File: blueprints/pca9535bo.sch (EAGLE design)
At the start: 8 parts, among them IC1 PCA9535D, J1 0R, J2 0R, J3 0R

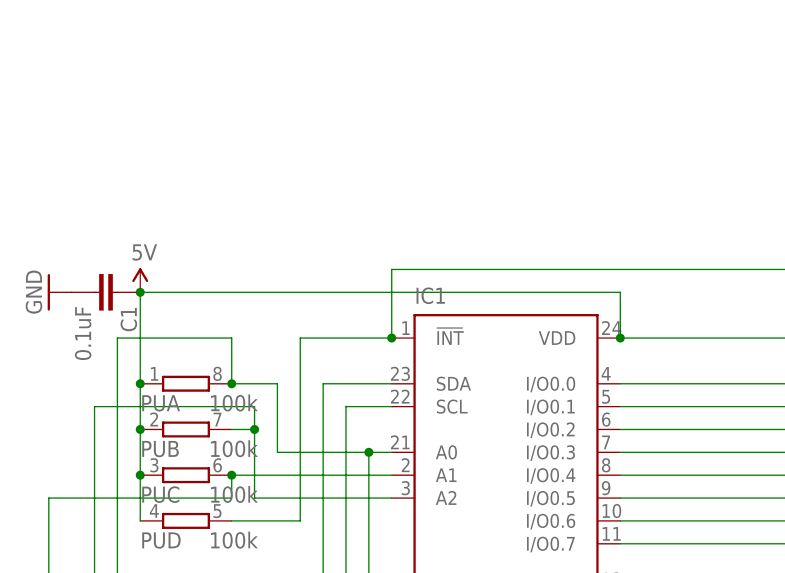
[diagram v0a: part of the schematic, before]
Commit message: I2C pullups and sizing down
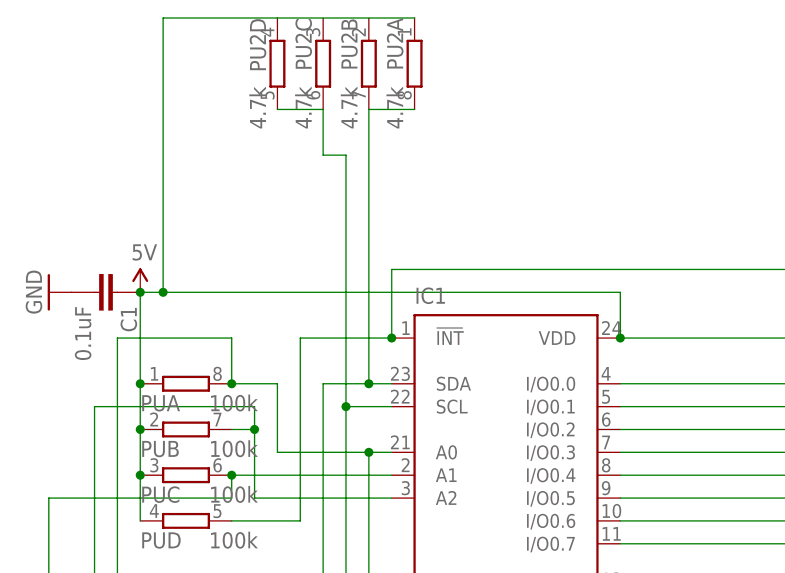
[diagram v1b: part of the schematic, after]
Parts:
- added PU2: 4.7k, resistor-dil:4R-NCAY16
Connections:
- net 5V: now also PU2A.1, PU2D.1
- net SCL: now also PU2C.2, PU2D.2
- net SDA: now also PU2A.2, PU2B.2
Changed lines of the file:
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@@
 <part name="J2" library="resistor" deviceset="R-EU_" device="R0603" value="0R"/>
 <part name="J3" library="resistor" deviceset="R-EU_" device="R0603" value="0R"/>
+<part name="PU2" library="resistor-dil" deviceset="4R-N" device="CAY16" value="4.7k"/>
 </parts>
 <sheets>
@@
 <instance part="J2" gate="G$1" x="25.4" y="147.32"/>
 <instance part="J3" gate="G$1" x="25.4" y="142.24"/>
+<instance part="PU2" gate="A" x="50.8" y="213.36" rot="R270"/>
+<instance part="PU2" gate="B" x="45.72" y="213.36" rot="R270"/>
+<instance part="PU2" gate="C" x="40.64" y="213.36" rot="R270"/>
+<instance part="PU2" gate="D" x="35.56" y="213.36" rot="R270"/>
 </instances>
 <busses>
@@
 <pinref part="PB" gate="G$1" pin="10"/>
 <wire x1="81.28" y1="132.08" x2="96.52" y2="132.08" width="0.1524" layer="91"/>
+<wire x1="43.18" y1="175.26" x2="43.18" y2="203.2" width="0.1524" layer="91"/>
+<pinref part="PU2" gate="C" pin="2"/>
+<wire x1="43.18" y1="203.2" x2="40.64" y2="203.2" width="0.1524" layer="91"/>
+<wire x1="40.64" y1="203.2" x2="40.64" y2="208.28" width="0.1524" layer="91"/>
+<pinref part="PU2" gate="D" pin="2"/>
+<wire x1="40.64" y1="208.28" x2="35.56" y2="208.28" width="0.1524" layer="91"/>
+<junction x="43.18" y="175.26"/>
 </segment>
 </net>
@@
 <segment>
 <pinref part="IC1" gate="G$1" pin="SDA"/>
-<wire x1="48.26" y1="177.8" x2="40.64" y2="177.8" width="0.1524" layer="91"/>
+<wire x1="48.26" y1="177.8" x2="45.72" y2="177.8" width="0.1524" layer="91"/>
+<wire x1="45.72" y1="177.8" x2="40.64" y2="177.8" width="0.1524" layer="91"/>
 <wire x1="40.64" y1="177.8" x2="40.64" y2="119.38" width="0.1524" layer="91"/>
 <wire x1="40.64" y1="119.38" x2="83.82" y2="119.38" width="0.1524" layer="91"/>
@@
 <pinref part="PB" gate="G$1" pin="11"/>
 <wire x1="83.82" y1="129.54" x2="96.52" y2="129.54" width="0.1524" layer="91"/>
+<pinref part="PU2" gate="B" pin="2"/>
+<wire x1="45.72" y1="177.8" x2="45.72" y2="208.28" width="0.1524" layer="91"/>
+<pinref part="PU2" gate="A" pin="2"/>
+<wire x1="45.72" y1="208.28" x2="50.8" y2="208.28" width="0.1524" layer="91"/>
+<junction x="45.72" y="177.8"/>
 </segment>
 </net>
@@
 <pinref part="PU" gate="C" pin="1"/>
 <junction x="20.32" y="167.64"/>
-<wire x1="73.66" y1="187.96" x2="20.32" y2="187.96" width="0.1524" layer="91"/>
+<wire x1="73.66" y1="187.96" x2="22.86" y2="187.96" width="0.1524" layer="91"/>
+<wire x1="22.86" y1="187.96" x2="20.32" y2="187.96" width="0.1524" layer="91"/>
 <wire x1="20.32" y1="187.96" x2="20.32" y2="177.8" width="0.1524" layer="91"/>
 <pinref part="U$1" gate="G$1" pin="5V"/>
@@
 <junction x="73.66" y="182.88"/>
 <pinref part="C1" gate="G$1" pin="1"/>
-</segment>
-</net>
+<pinref part="PU2" gate="A" pin="1"/>
+<pinref part="PU2" gate="D" pin="1"/>
+<wire x1="50.8" y1="218.44" x2="35.56" y2="218.44" width="0.1524" layer="91"/>
+<wire x1="35.56" y1="218.44" x2="22.86" y2="218.44" width="0.1524" layer="91"/>
+<wire x1="22.86" y1="218.44" x2="22.86" y2="187.96" width="0.1524" layer="91"/>
+<junction x="22.86" y="187.96"/>
+</segment>
+</net>

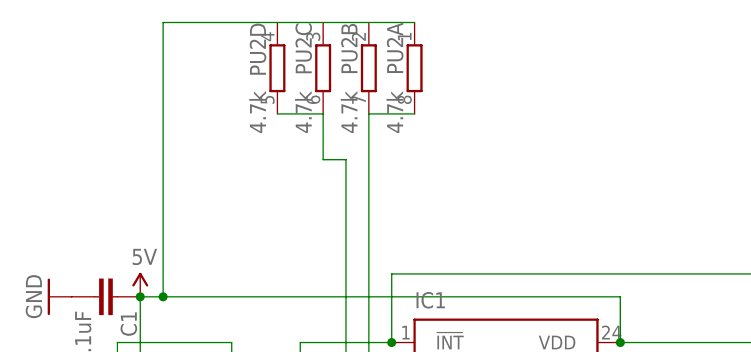
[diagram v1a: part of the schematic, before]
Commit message: forgot some junction
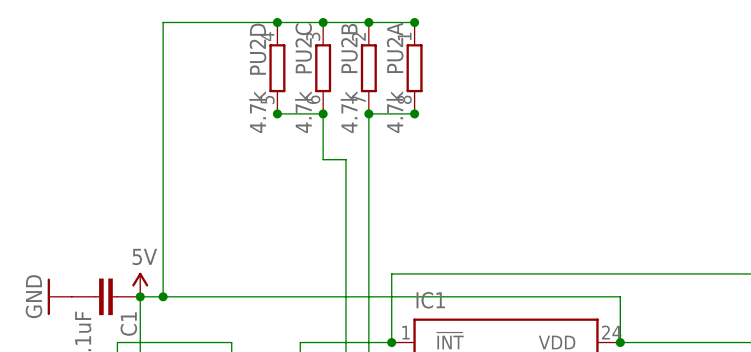
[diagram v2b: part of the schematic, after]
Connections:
- net 5V: now also PU2B.1, PU2C.1
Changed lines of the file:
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@@
 <wire x1="40.64" y1="208.28" x2="35.56" y2="208.28" width="0.1524" layer="91"/>
 <junction x="43.18" y="175.26"/>
+<junction x="40.64" y="208.28"/>
+<junction x="35.56" y="208.28"/>
 </segment>
 </net>
@@
 <wire x1="45.72" y1="208.28" x2="50.8" y2="208.28" width="0.1524" layer="91"/>
 <junction x="45.72" y="177.8"/>
+<junction x="50.8" y="208.28"/>
+<junction x="45.72" y="208.28"/>
 </segment>
 </net>
@@
 <pinref part="PU2" gate="A" pin="1"/>
 <pinref part="PU2" gate="D" pin="1"/>
-<wire x1="50.8" y1="218.44" x2="35.56" y2="218.44" width="0.1524" layer="91"/>
+<wire x1="50.8" y1="218.44" x2="45.72" y2="218.44" width="0.1524" layer="91"/>
+<wire x1="45.72" y1="218.44" x2="40.64" y2="218.44" width="0.1524" layer="91"/>
+<wire x1="40.64" y1="218.44" x2="35.56" y2="218.44" width="0.1524" layer="91"/>
 <wire x1="35.56" y1="218.44" x2="22.86" y2="218.44" width="0.1524" layer="91"/>
 <wire x1="22.86" y1="218.44" x2="22.86" y2="187.96" width="0.1524" layer="91"/>
 <junction x="22.86" y="187.96"/>
+<junction x="35.56" y="218.44"/>
+<pinref part="PU2" gate="C" pin="1"/>
+<junction x="40.64" y="218.44"/>
+<pinref part="PU2" gate="B" pin="1"/>
+<junction x="45.72" y="218.44"/>
+<junction x="50.8" y="218.44"/>
 </segment>
 </net>

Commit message: some clarificationt texts
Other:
- note added: "I2C pull-up, optional"
- note added: "address & int- pullups"
- note added: "address solder jumpers, optional"
- note added: "bypass C"
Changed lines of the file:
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@@
 <sheet>
 <plain>
+<text x="30.48" y="223.52" size="1.778" layer="91">I2C pull-up, optional</text>
+<text x="-7.62" y="134.62" size="1.778" layer="91">address solder jumpers, optional</text>
+<text x="-10.16" y="170.18" size="1.778" layer="91">address &amp; int- pullups</text>
+<text x="7.62" y="195.58" size="1.778" layer="91">bypass C</text>
 </plain>
 <instances>
